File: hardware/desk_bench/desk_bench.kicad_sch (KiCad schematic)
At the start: 1 part, among them J1 Raspberry_Pi_2_3

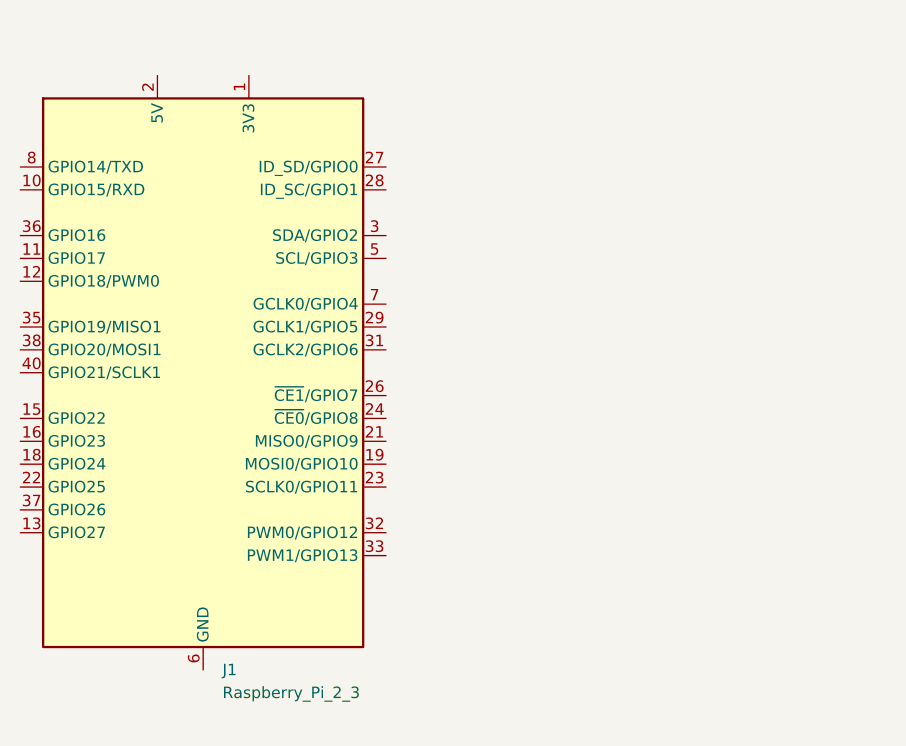
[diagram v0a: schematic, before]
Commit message: hardware: GY-6500 symbol in drone_parts library, placed next to Pi
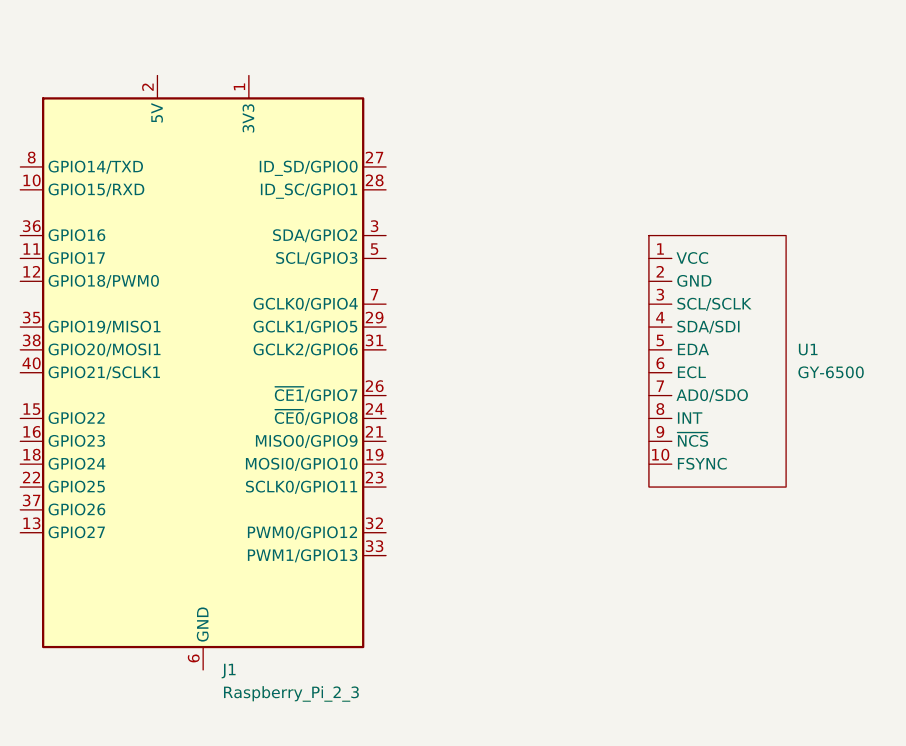
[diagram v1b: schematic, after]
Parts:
- added U1: GY-6500, symbol drone_parts:GY-6500
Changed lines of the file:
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@@
 	(paper "A4")
+	(symbol
+		(lib_id "drone_parts:GY-6500")
+		(at 195.58 85.09 0)
+		(unit 1)
+		(body_style 1)
+		(exclude_from_sim no)
+		(in_bom yes)
+		(on_board yes)
+		(in_pos_files yes)
+		(dnp no)
+		(fields_autoplaced yes)
+		(property "Reference" "U1"
+			(at 204.47 80.0099 0)
+			(show_name no)
+			(do_not_autoplace no)
+			(effects
+				(font
+					(size 1.27 1.27)
+				)
+				(justify left)
+			)
+		)
+		(property "Value" "GY-6500"
+			(at 204.47 82.5499 0)
+			(show_name no)
+			(do_not_autoplace no)
+			(effects
+				(font
+					(size 1.27 1.27)
+				)
+				(justify left)
+			)
+		)
+		(property "Footprint" ""
+			(at 195.58 85.09 0)
+			(hide yes)
+			(show_name no)
+			(do_not_autoplace no)
+			(effects
+				(font
+					(size 1.27 1.27)
+				)
+			)
+		)
+		(property "Datasheet" ""
+			(at 195.58 85.09 0)
+			(hide yes)
+			(show_name no)
+			(do_not_autoplace no)
+			(effects
+				(font
+					(size 1.27 1.27)
+				)
+			)
+		)
+		(property "Description" "MPU-6500 6-axis IMU breakout, SPI or I2C"
+			(at 195.58 85.09 0)
+			(hide yes)
+			(show_name no)
+			(do_not_autoplace no)
+			(effects
+				(font
+					(size 1.27 1.27)
+				)
+			)
+		)
+		(pin "3"
+		)
+		(pin "1"
+		)
+		(pin "2"
+		)
+		(pin "10"
+		)
+		(pin "9"
+		)
+		(pin "5"
+		)
+		(pin "4"
+		)
+		(pin "8"
+		)
+		(pin "7"
+		)
+		(pin "6"
+		)
+		(instances
+			(project "desk_bench"
+				(path "/531ea3af-daec-4a92-b36d-328eca773792"
+					(reference "U1")
+					(unit 1)
+				)
+			)
+		)
+	)
 	(symbol
 		(lib_id "Connector:Raspberry_Pi_2_3")

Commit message: hardware: desk_bench power symbols + SPI wiring
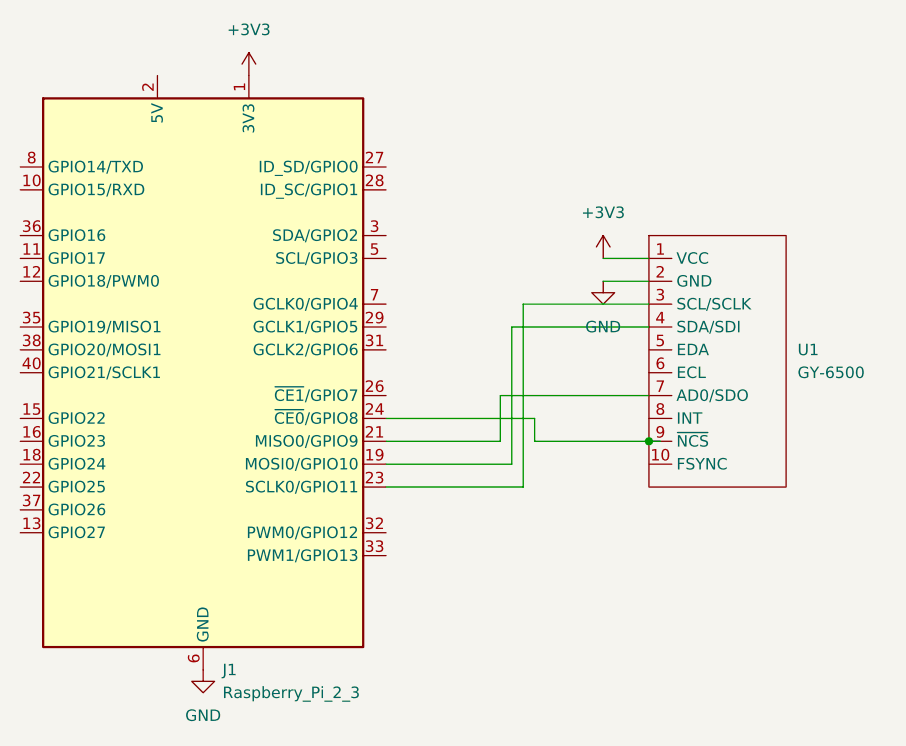
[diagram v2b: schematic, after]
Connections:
- net +3V3: now reaches U1.1 (VCC)
- net +3V3: now also J1.1 (3V3), J1.17 (3V3)
- net GND: now reaches U1.2 (GND)
- net GND: now also J1.14 (GND), J1.20 (GND), J1.25 (GND), J1.30 (GND), J1.34 (GND), J1.39 (GND), J1.6 (GND), J1.9 (GND)
- net at U1.3 (SCL/SCLK): now also J1.23 (SCLK0/GPIO11)
- net at U1.4 (SDA/SDI): now also J1.19 (MOSI0/GPIO10)
- net at U1.7 (AD0/SDO): now also J1.21 (MISO0/GPIO9)
- net at U1.9 (~{NCS}): now also J1.24 (~{CE0}/GPIO8)
